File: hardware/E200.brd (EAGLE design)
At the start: 38.1 x 32.5 mm, 26 parts, among them SW1 SPST_TACT-KMR2, U11 915MHz, U5 ATMEGA328P-MU, U8 MCP1703CB, X1 16 MHz

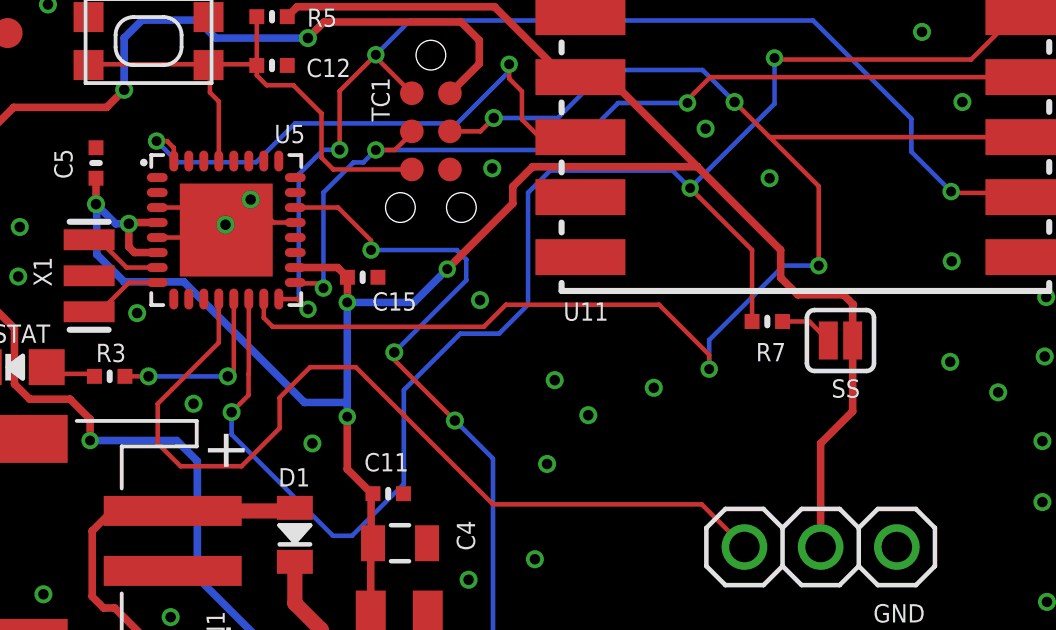
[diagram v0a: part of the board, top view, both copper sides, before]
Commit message: v1.1.0 - small update
- added silkscreen to bottom for node id
- solder mask DRU for covering vias
- removed solder jumper
- minor trace adjustments
- functionally same as previous
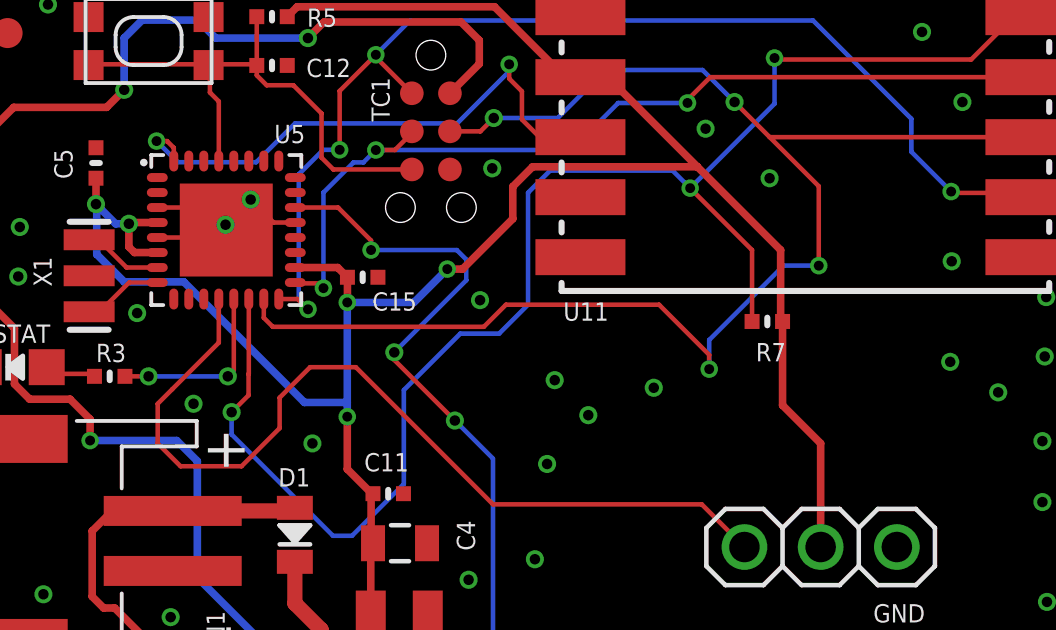
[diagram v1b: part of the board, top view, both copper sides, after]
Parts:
- removed SS: JUMPER-SMT_2_NC_PASTE_SILK, SparkFun-Jumpers:SMT-JUMPER_2_NC_PASTE_SILK
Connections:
- removed net N$11: R7.2, SS.2
- net VCC: now also R7.2; no longer SS.1
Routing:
- net N$11: track 1.79 -> 0.00 mm
- net VCC: track 76.6 -> 75.1 mm
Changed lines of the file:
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@@
 <?xml version="1.0" encoding="utf-8"?>
 <!DOCTYPE eagle SYSTEM "eagle.dtd">
-<eagle version="9.4.1">
+<eagle version="9.5.1">
 <drawing>
 <settings>
@@
 <text x="36.195" y="44.1198" size="0.6096" layer="122" font="vector" rot="MR0" align="bottom-center">E200</text>
 <text x="31.5722" y="48.387" size="0.6096" layer="121" font="vector" align="bottom-center">GND</text>
+<polygon width="0.1524" layer="122">
+<vertex x="0.508" y="45.466"/>
+<vertex x="20.574" y="45.466"/>
+<vertex x="20.574" y="55.626"/>
+<vertex x="0.508" y="55.626"/>
+</polygon>
 </plain>
 <attributes>
@@
 </class>
 </classes>
-<designrules name="oshpark-2layer">
+<designrules name="oshpark-2layer *">
 <description language="en">&lt;b&gt;OSH Park Design Rules&lt;/b&gt;
 &lt;p&gt;
@@
 <param name="mlMinCreamFrame" value="0mil"/>
 <param name="mlMaxCreamFrame" value="0mil"/>
-<param name="mlViaStopLimit" value="0mil"/>
+<param name="mlViaStopLimit" value="14mil"/>
 <param name="srRoundness" value="0"/>
 <param name="srMinRoundness" value="0mil"/>
@@
 <attribute name="VALUE" x="25.146" y="47.7266" size="1.27" layer="27"/>
 </element>
-<element name="SS" library="SparkFun-Jumpers" package="SMT-JUMPER_2_NC_PASTE_SILK" value="JUMPER-SMT_2_NC_PASTE_SILK" x="29.6164" y="57.785" smashed="yes" rot="R180">
-<attribute name="NAME" x="29.7942" y="55.88" size="0.6096" layer="121" font="vector" align="bottom-center"/>
-</element>
 <element name="D1" library="SCHOTTKY_0805" package="0805" value="" x="11.43" y="51.308" smashed="yes" rot="R270">
 <attribute name="NAME" x="11.938" y="53.5305" size="0.6096" layer="121" font="vector" rot="R180"/>
@@
 <wire x1="13.97" y1="52.705" x2="13.17625" y2="53.49875" width="0.254" layer="1"/>
 <wire x1="13.97" y1="52.705" x2="14.0335" y2="52.6796" width="0.1524" layer="1"/>
-<wire x1="11.7475" y1="55.72125" x2="8.245475" y2="59.223275" width="0.254" layer="16"/>
+<wire x1="11.7475" y1="55.72125" x2="7.72795" y2="59.7408" width="0.254" layer="16"/>
 <wire x1="13.17625" y1="55.72125" x2="11.7475" y2="55.72125" width="0.254" layer="16"/>
 <wire x1="20.32" y1="66.675" x2="18.0848" y2="68.9102" width="0.254" layer="1"/>
@@
 <wire x1="11.444" y1="60.218" x2="12.8578" y2="60.218" width="0.254" layer="1"/>
 <wire x1="12.8578" y1="60.218" x2="13.1826" y2="59.8932" width="0.254" layer="1"/>
-<wire x1="8.245475" y1="59.223275" x2="7.72795" y2="59.7408" width="0.254" layer="16"/>
 <wire x1="5.7404" y1="59.7408" x2="4.826" y2="60.6552" width="0.254" layer="16"/>
 <wire x1="4.826" y1="60.6552" x2="4.826" y2="62.3062" width="0.254" layer="16"/>
@@
 <wire x1="13.9598" y1="48.7504" x2="13.9598" y2="50.9532" width="0.254" layer="1"/>
 <wire x1="13.9598" y1="50.9532" x2="14.0352" y2="51.0286" width="0.1524" layer="1"/>
-<wire x1="16.51" y1="60.16625" x2="18.6944" y2="62.35065" width="0.254" layer="1"/>
-<wire x1="18.6944" y1="62.9158" x2="18.6944" y2="62.35065" width="0.254" layer="1"/>
+<wire x1="16.51" y1="60.16625" x2="17.018" y2="60.16625" width="0.254" layer="1"/>
+<wire x1="18.6944" y1="61.84265" x2="17.018" y2="60.16625" width="0.254" layer="1"/>
+<wire x1="18.6944" y1="62.9158" x2="18.6944" y2="61.84265" width="0.254" layer="1"/>
 <wire x1="19.3548" y1="63.5762" x2="18.6944" y2="62.9158" width="0.254" layer="1"/>
 <wire x1="24.84755" y1="63.5762" x2="19.3548" y2="63.5762" width="0.254" layer="1"/>
@@
 <wire x1="5.93800625" y1="61.718" x2="5.896815625" y2="61.676809375" width="0.254" layer="1"/>
 <contactref element="JP2" pad="2"/>
-<contactref element="SS" pad="1"/>
-<wire x1="27.6225" y1="59.8805" x2="28.194" y2="59.309" width="0.254" layer="1"/>
-<wire x1="28.194" y1="59.309" x2="29.718" y2="59.309" width="0.254" layer="1"/>
-<wire x1="29.718" y1="59.309" x2="30.0482" y2="58.9788" width="0.254" layer="1"/>
-<wire x1="30.0482" y1="58.9788" x2="30.0228" y2="58.9534" width="0.254" layer="1"/>
-<wire x1="30.0228" y1="58.9534" x2="30.0228" y2="57.785" width="0.254" layer="1"/>
-<wire x1="27.6225" y1="60.80125" x2="27.6225" y2="59.8805" width="0.254" layer="1"/>
 <wire x1="28.956" y1="54.356" x2="28.956" y2="50.9016" width="0.254" layer="1"/>
-<wire x1="30.0228" y1="57.785" x2="30.0228" y2="55.4228" width="0.254" layer="1"/>
-<wire x1="30.0228" y1="55.4228" x2="28.956" y2="54.356" width="0.254" layer="1"/>
+<contactref element="R7" pad="2"/>
+<wire x1="27.6225" y1="58.4835" x2="27.686" y2="58.42" width="0.254" layer="1"/>
+<wire x1="27.6225" y1="60.80125" x2="27.6225" y2="58.4835" width="0.254" layer="1"/>
+<wire x1="27.686" y1="58.42" x2="27.686" y2="55.626" width="0.254" layer="1"/>
+<wire x1="27.686" y1="55.626" x2="28.956" y2="54.356" width="0.254" layer="1"/>
 </signal>
 <signal name="SCL">
@@
 <wire x1="3.175" y1="56.8325" x2="3.1582" y2="56.896" width="0.1524" layer="1"/>
 </signal>
-<signal name="N$11">
-<contactref element="R7" pad="2"/>
-<contactref element="SS" pad="2"/>
-<wire x1="27.686" y1="58.42" x2="28.575" y2="58.42" width="0.1524" layer="1"/>
-<wire x1="28.575" y1="58.42" x2="29.21" y2="57.785" width="0.1524" layer="1"/>
-</signal>
 </signals>
